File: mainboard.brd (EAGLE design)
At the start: 90.2 x 95.9 mm, 69 parts, among them T1 SINGLE_NCHAN_FET, T2 MOSFET_PCHAN_20A, T3 SINGLE_NCHAN_FET, T4 MOSFET_PCHAN_20A, T5 SINGLE_NCHAN_FET, T6 MOSFET_PCHAN_20A, U1 MURATA_REG_OKL-T3-W12, U2 TEENSY_3.0+4, U3 RFM23BP, U4 HMC5883LSMD, U5 ITG-3200, U6 AB0805, U7 CURRENT_MAX4372, U8 CURRENT_MAX4372, X1 CRYSTAL.ABS07

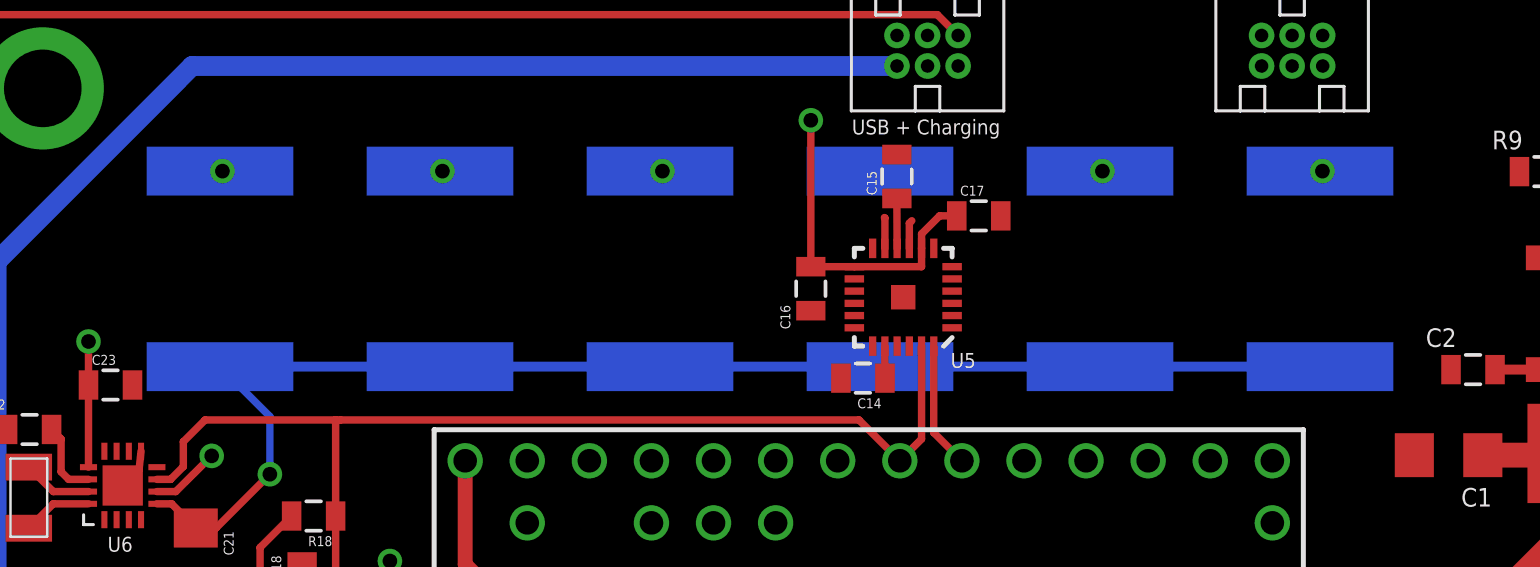
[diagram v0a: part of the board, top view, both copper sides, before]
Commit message: Removed beta batteries
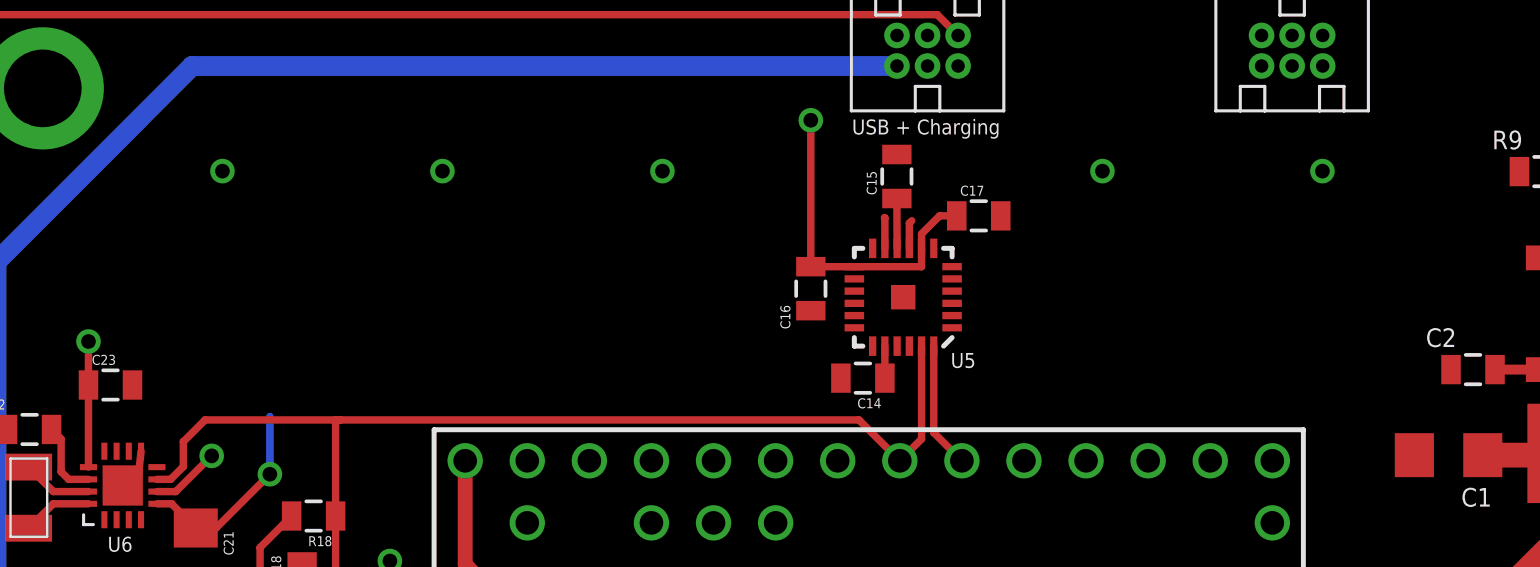
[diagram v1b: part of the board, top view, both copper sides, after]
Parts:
- removed B1, B2, B3, B4, B5, B6: BETABATTERY, Widetronix:BETABATTERY
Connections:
- removed net VBACKUP: B1.V+, B2.V+, B3.V+, B4.V+, B5.V+, B6.V+, C21.1, U6.VBAT
- net 3.3V: now also C21.1, U6.VBAT
- net GND: no longer B1.V-, B2.V-, B3.V-, B4.V-, B5.V-, B6.V-
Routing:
- net VBACKUP: track 56.2 -> 0.00 mm, vias 1 -> 0
- net 3.3V: track 36.6 -> 44.9 mm, vias 6 -> 7
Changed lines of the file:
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@@
 <element name="G1" library="G125-FV20605L0P" package="G125-FV20605L0P" value="G125-FV20605L0P" x="60" y="89.885"/>
 <element name="G2" library="G125-FV20605L0P" package="G125-FV20605L0P" value="G125-FV20605L0P" x="84.17" y="47.9425" rot="R270"/>
-<element name="B1" library="Widetronix" package="BETABATTERY" value="BETABATTERY" x="61.24" y="83.42" rot="MR90"/>
-<element name="B2" library="Widetronix" package="BETABATTERY" value="BETABATTERY" x="52.24" y="83.42" rot="MR90"/>
-<element name="B3" library="Widetronix" package="BETABATTERY" value="BETABATTERY" x="43.24" y="83.42" rot="MR90"/>
-<element name="B4" library="Widetronix" package="BETABATTERY" value="BETABATTERY" x="34.24" y="83.42" rot="MR90"/>
-<element name="B5" library="Widetronix" package="BETABATTERY" value="BETABATTERY" x="25.24" y="83.42" rot="MR90"/>
-<element name="B6" library="Widetronix" package="BETABATTERY" value="BETABATTERY" x="16.24" y="83.42" rot="MR90"/>
 <element name="ST1" library="SparkFun-Connectors" package="SCREWTERMINAL-3.5MM-2_LOCK" value="M023.5MM_LOCK" x="12.09" y="17.61" smashed="yes" rot="R270"/>
 <element name="ST2" library="SparkFun-Connectors" package="SCREWTERMINAL-3.5MM-2_LOCK" value="M023.5MM_LOCK" x="12.09" y="24.61" smashed="yes" rot="R270"/>
@@
 <via x="85.09" y="5.08" extent="1-16" drill="3.175" diameter="5"/>
 <via x="5.09" y="5.08" extent="1-16" drill="3.175" diameter="5"/>
-<contactref element="B1" pad="V-"/>
-<contactref element="B2" pad="V-"/>
-<contactref element="B3" pad="V-"/>
-<contactref element="B4" pad="V-"/>
-<contactref element="B5" pad="V-"/>
-<contactref element="B6" pad="V-"/>
 <contactref element="ST1" pad="1"/>
 <contactref element="ST2" pad="1"/>
@@
 <wire x1="19.5" y1="71.43" x2="19.12" y2="67.05" width="0" layer="19" extent="1-1"/>
 </signal>
-<signal name="VBACKUP">
-<contactref element="B1" pad="V+"/>
-<contactref element="B2" pad="V+"/>
-<contactref element="B3" pad="V+"/>
-<contactref element="B4" pad="V+"/>
-<contactref element="B5" pad="V+"/>
-<contactref element="B6" pad="V+"/>
-<contactref element="U6" pad="VBAT"/>
-<contactref element="C21" pad="1"/>
-<wire x1="16.14" y1="79.42" x2="25.14" y2="79.42" width="0.4064" layer="16"/>
-<wire x1="25.14" y1="79.42" x2="34.14" y2="79.42" width="0.4064" layer="16"/>
-<wire x1="34.14" y1="79.42" x2="43.14" y2="79.42" width="0.4064" layer="16"/>
-<wire x1="43.14" y1="79.42" x2="52.14" y2="79.42" width="0.4064" layer="16"/>
-<wire x1="61.14" y1="79.42" x2="52.14" y2="79.42" width="0.4064" layer="16"/>
-<wire x1="13.56" y1="73.81" x2="14.16" y2="73.81" width="0.3048" layer="1"/>
-<wire x1="14.16" y1="73.81" x2="15.15" y2="72.82" width="0.3048" layer="1"/>
-<via x="18.18" y="75.02" extent="1-16" drill="0.6"/>
-<wire x1="15.15" y1="72.82" x2="15.98" y2="72.82" width="0.3048" layer="1"/>
-<wire x1="15.98" y1="72.82" x2="18.18" y2="75.02" width="0.3048" layer="1"/>
-<wire x1="18.18" y1="75.02" x2="18.18" y2="77.38" width="0.3048" layer="16"/>
-<wire x1="18.18" y1="77.38" x2="16.14" y2="79.42" width="0.3048" layer="16"/>
-</signal>
 <signal name="VREG_IN">
 <contactref element="U7" pad="5"/>
@@
 <contactref element="U2" pad="3.3V"/>
 <contactref element="U2" pad="3.3V1"/>
+<contactref element="U6" pad="VBAT"/>
+<contactref element="C21" pad="1"/>
+<wire x1="13.56" y1="73.81" x2="14.16" y2="73.81" width="0.3048" layer="1"/>
+<wire x1="14.16" y1="73.81" x2="15.15" y2="72.82" width="0.3048" layer="1"/>
+<via x="18.18" y="75.02" extent="1-16" drill="0.6"/>
+<wire x1="15.15" y1="72.82" x2="15.98" y2="72.82" width="0.3048" layer="1"/>
+<wire x1="15.98" y1="72.82" x2="18.18" y2="75.02" width="0.3048" layer="1"/>
+<wire x1="18.18" y1="75.02" x2="18.18" y2="77.38" width="0.3048" layer="16"/>
 </signal>
 <signal name="5V">

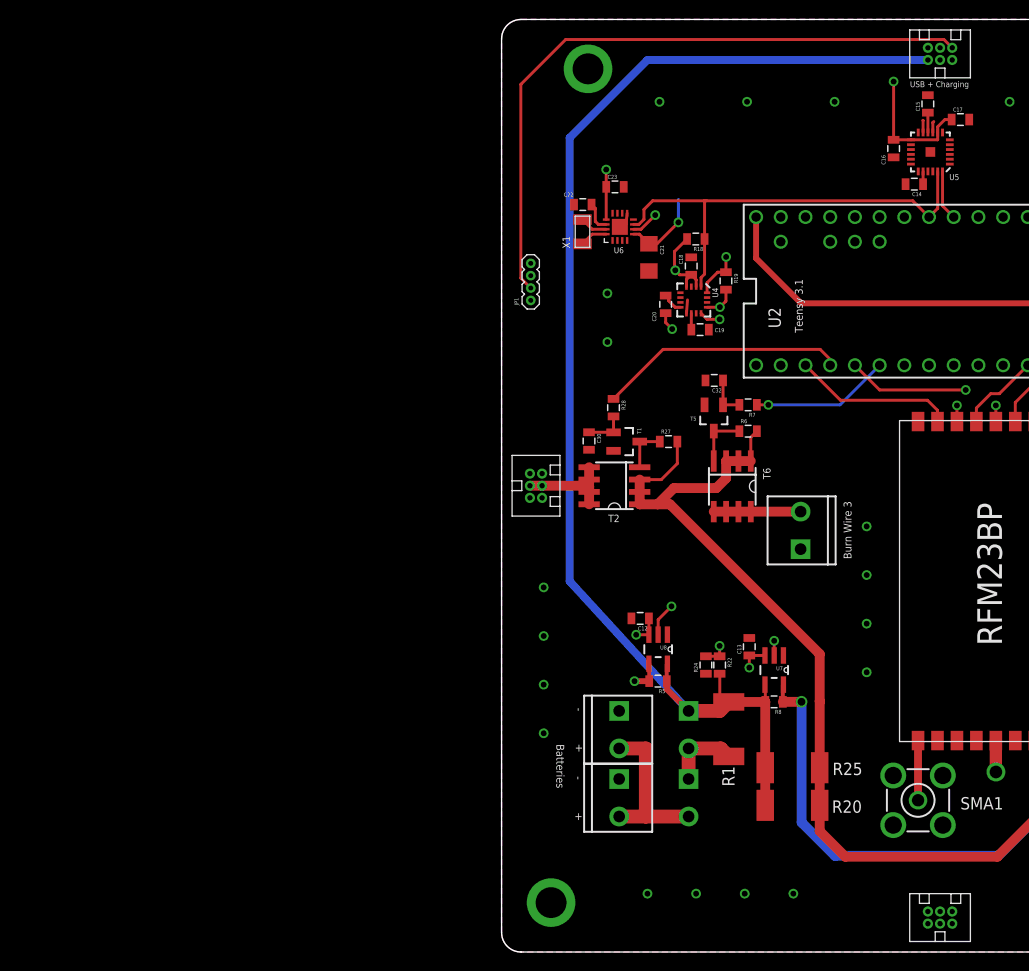
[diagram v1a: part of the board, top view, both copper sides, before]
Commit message: New solar panel design
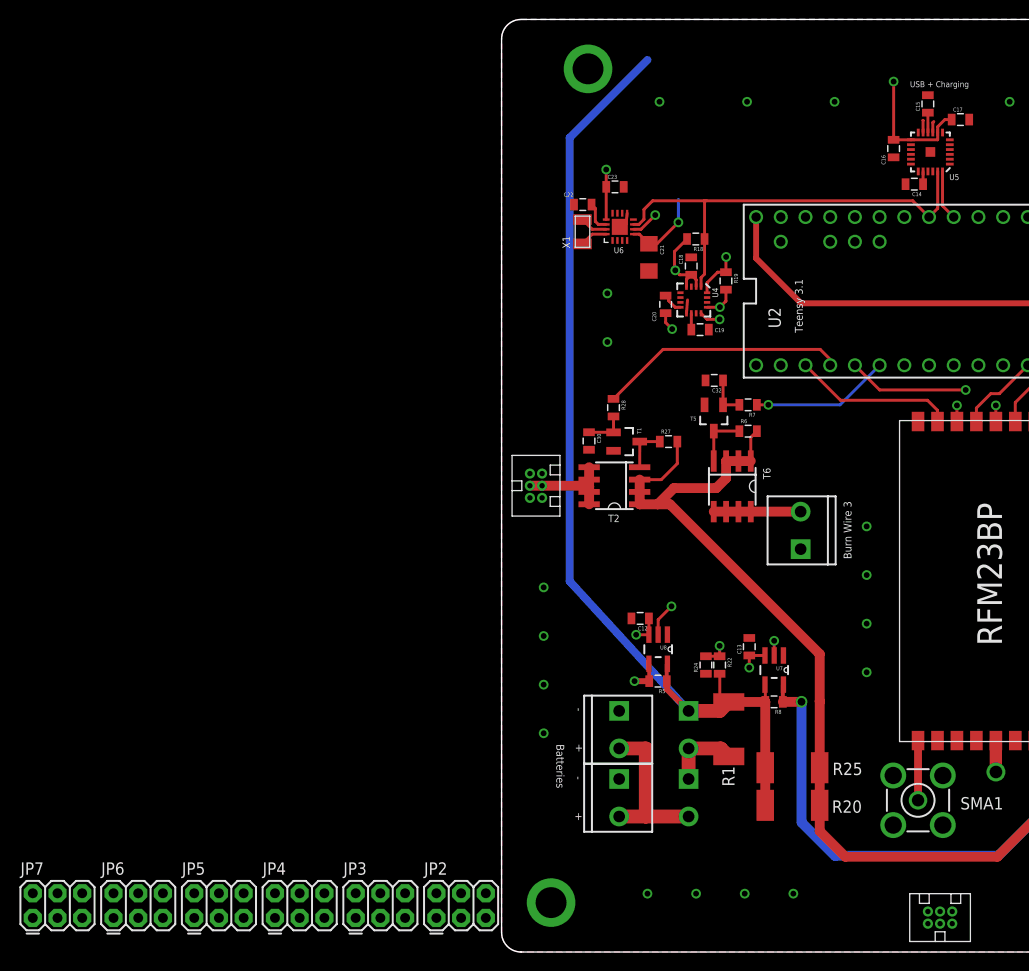
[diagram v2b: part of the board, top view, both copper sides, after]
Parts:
- removed G7: G125-FV20605L0P, G125-FV20605L0P:G125-FV20605L0P
- removed JP1: (no value), SparkFun-Connectors:1X04-1.27MM
- added JP2, JP3, JP4, JP5, JP6, JP7: (no value), SparkFun-Connectors:2X3
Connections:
- removed net D+: G7.P4, JP1.2
- removed net D-: G7.P1, JP1.3
- removed net ID: G7.P5
- removed net VBUS: G7.P2, JP1.4
- net GND: now also JP2.2, JP3.2, JP4.2, JP5.2, JP6.2, JP7.2; no longer G7.P6, JP1.1
- net VBATT: no longer G7.P3
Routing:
- net D+: track 68.0 -> 0.00 mm
- net D-: track 57.7 -> 0.00 mm
- net VBUS: track 55.2 -> 0.00 mm
- net VBATT: track 134.2 -> 105.3 mm
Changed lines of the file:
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@@
 </element>
 <element name="C23" library="SparkFun-Capacitors" package="0805" value="0.1uF" x="11.66" y="78.67"/>
-<element name="JP1" library="SparkFun-Connectors" package="1X04-1.27MM" value="" x="3" y="67" rot="R90"/>
-<element name="G7" library="G125-FV20605L0P" package="G125-FV20605L0P" value="G125-FV20605L0P" x="45.085" y="94.805" rot="R180"/>
 <element name="U1" library="phonesat" package="MURATA_REG_OKL-T6-W12" value="MURATA_REG_OKL-T3-W12" x="76.8" y="79.3" smashed="yes" rot="R180">
 <attribute name="NAME" x="85.829" y="77.129" size="1.27" layer="25" rot="R180"/>
@@
 <attribute name="VALUE" x="84.176" y="68.197" size="0.4064" layer="27" rot="R270"/>
 </element>
+<element name="JP2" library="SparkFun-Connectors" package="2X3" value="" x="-6.7" y="3.5"/>
+<element name="JP3" library="SparkFun-Connectors" package="2X3" value="" x="-15" y="3.5"/>
+<element name="JP4" library="SparkFun-Connectors" package="2X3" value="" x="-23.3" y="3.5"/>
+<element name="JP5" library="SparkFun-Connectors" package="2X3" value="" x="-31.6" y="3.5"/>
+<element name="JP6" library="SparkFun-Connectors" package="2X3" value="" x="-39.9" y="3.5"/>
+<element name="JP7" library="SparkFun-Connectors" package="2X3" value="" x="-48.2" y="3.5"/>
 </elements>
 <signals>
@@
 <wire x1="12.79" y1="74.83" x2="12.16" y2="74.56" width="0.3048" layer="1"/>
 <contactref element="C23" pad="2"/>
-<contactref element="G7" pad="P6"/>
-<contactref element="JP1" pad="1"/>
 <via x="15" y="6" extent="1-16" drill="0.6"/>
 <via x="20" y="6" extent="1-16" drill="0.6"/>
@@
 <contactref element="C2" pad="2"/>
 <contactref element="C3" pad="2"/>
+<contactref element="JP2" pad="2"/>
+<contactref element="JP3" pad="2"/>
+<contactref element="JP4" pad="2"/>
+<contactref element="JP5" pad="2"/>
+<contactref element="JP6" pad="2"/>
+<contactref element="JP7" pad="2"/>
+<wire x1="-39.9" y1="6.04" x2="-48.2" y2="6.04" width="0" layer="19" extent="1-1"/>
+<wire x1="-31.6" y1="6.04" x2="-39.9" y2="6.04" width="0" layer="19" extent="1-1"/>
+<wire x1="-23.3" y1="6.04" x2="-31.6" y2="6.04" width="0" layer="19" extent="1-1"/>
+<wire x1="-15" y1="6.04" x2="-23.3" y2="6.04" width="0" layer="19" extent="1-1"/>
+<wire x1="-6.7" y1="6.04" x2="-15" y2="6.04" width="0" layer="19" extent="1-1"/>
+<wire x1="5.09" y1="5.08" x2="-6.7" y2="6.04" width="0" layer="19" extent="1-1"/>
 <wire x1="19.5" y1="71.43" x2="19.12" y2="67.05" width="0" layer="19" extent="1-1"/>
 </signal>
@@
 <wire x1="27.12" y1="25.72" x2="27.11" y2="25.72" width="1.016" layer="1"/>
 <wire x1="27.11" y1="25.72" x2="27.11" y2="18.95" width="1.016" layer="1"/>
-<contactref element="G7" pad="P3"/>
-<wire x1="43.835" y1="91.72" x2="15" y2="91.72" width="0.8128" layer="16"/>
 <wire x1="15" y1="91.72" x2="7" y2="83.715" width="0.8128" layer="16"/>
 <wire x1="7" y1="83.715" x2="7" y2="38.1228" width="0.8128" layer="16"/>
@@
 <wire x1="32.71" y1="12.43" x2="32.71" y2="15.08" width="1.016" layer="1"/>
 </signal>
-<signal name="VBUS">
-<contactref element="G7" pad="P2"/>
-<contactref element="JP1" pad="4"/>
-<wire x1="3" y1="70.81" x2="3" y2="78.43" width="0.4064" layer="2"/>
-<wire x1="45.085" y1="91.72" x2="44.165" y2="90.8" width="0.4064" layer="2"/>
-<wire x1="44.165" y1="90.8" x2="15.37" y2="90.8" width="0.4064" layer="2"/>
-<wire x1="15.37" y1="90.8" x2="3" y2="78.43" width="0.4064" layer="2"/>
-</signal>
-<signal name="D-">
-<contactref element="G7" pad="P1"/>
-<contactref element="JP1" pad="3"/>
-<wire x1="3" y1="69.54" x2="4.08" y2="70.62" width="0.4064" layer="15"/>
-<wire x1="4.08" y1="70.62" x2="4.08" y2="79.51" width="0.4064" layer="15"/>
-<wire x1="4.08" y1="79.51" x2="15.37" y2="90.8" width="0.4064" layer="15"/>
-<wire x1="15.37" y1="90.8" x2="45.415" y2="90.8" width="0.4064" layer="15"/>
-<wire x1="45.415" y1="90.8" x2="46.335" y2="91.72" width="0.4064" layer="15"/>
-</signal>
-<signal name="ID">
-<contactref element="G7" pad="P5"/>
-</signal>
-<signal name="D+">
-<contactref element="G7" pad="P4"/>
-<contactref element="JP1" pad="2"/>
-<wire x1="46.335" y1="92.97" x2="45.485" y2="93.82" width="0.3048" layer="1"/>
-<wire x1="45.485" y1="93.82" x2="6.59" y2="93.82" width="0.3048" layer="1"/>
-<wire x1="6.59" y1="93.82" x2="1.98" y2="89.21" width="0.3048" layer="1"/>
-<wire x1="1.98" y1="89.21" x2="1.98" y2="69.29" width="0.3048" layer="1"/>
-<wire x1="3" y1="68.27" x2="1.98" y2="69.29" width="0.3048" layer="1"/>
-</signal>
 <signal name="N$1">

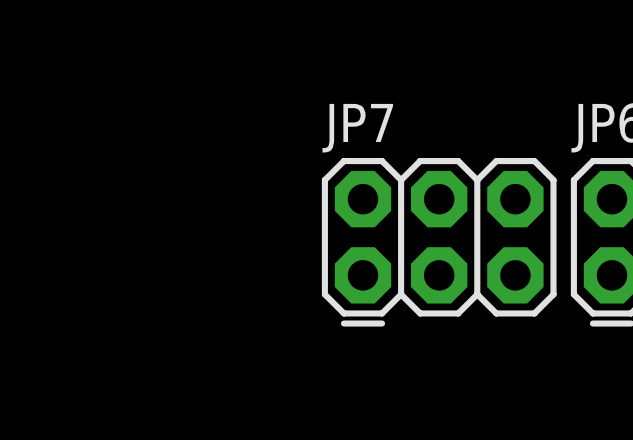
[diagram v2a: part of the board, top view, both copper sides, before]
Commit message: Added pull down resistors to burn wire circuits
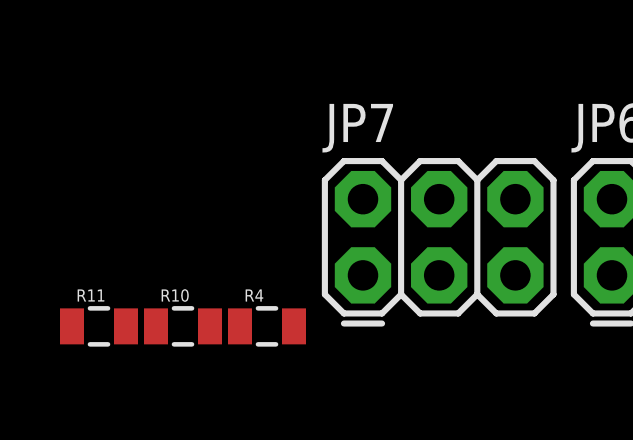
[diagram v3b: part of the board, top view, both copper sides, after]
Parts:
- added R10, R11, R4: 4.7K, SparkFun-Resistors:0805
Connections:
- net ENAB_BURN1: now also R4.2
- net ENAB_BURN2: now also R10.2
- net ENAB_BURN3: now also R11.2
- net GND: now also R10.1, R11.1, R4.1
